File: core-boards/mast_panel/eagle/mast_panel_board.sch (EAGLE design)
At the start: 30 parts, among them J1 2-PIN_2MM-V, J4 4-PIN_2MM-H, U1 ATMEGA328P-AUR, U3 MCP2551T-I/SN

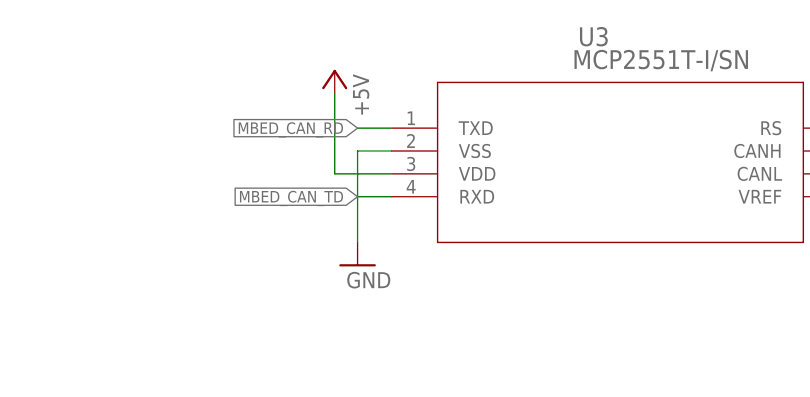
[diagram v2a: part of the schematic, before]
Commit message: 3/1/2020
Switched out CAN connector, cleaned up a few things
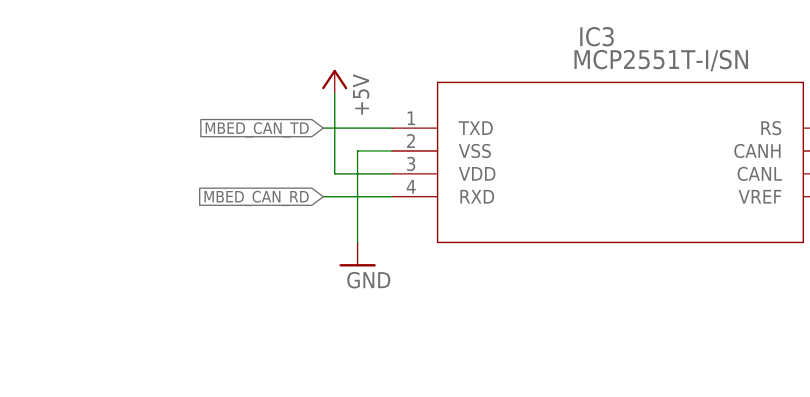
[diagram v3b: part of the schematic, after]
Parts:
- IC3: DIGIKEY (none) -> MCP2551T-I/SNCT-ND
- renumbered U3 to IC3
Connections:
- net MBED_CAN_RD: now also IC3.RXD; no longer IC3.TXD
- net MBED_CAN_TD: now also IC3.TXD; no longer IC3.RXD
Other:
- note added: "CAN Controller"
- note removed: "CAN Bus"
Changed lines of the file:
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@@
 <part name="GND11" library="supply1" library_urn="urn:adsk.eagle:library:371" deviceset="GND" device=""/>
 <part name="GND17" library="supply1" library_urn="urn:adsk.eagle:library:371" deviceset="GND" device=""/>
-<part name="U3" library="MCP2551T" deviceset="MCP2551T-I/SN" device=""/>
 <part name="GND18" library="supply1" library_urn="urn:adsk.eagle:library:371" deviceset="GND" device=""/>
 <part name="GND19" library="supply1" library_urn="urn:adsk.eagle:library:371" deviceset="GND" device=""/>
@@
 <part name="R9" library="rcl" library_urn="urn:adsk.eagle:library:334" deviceset="R-US_" device="R0805" package3d_urn="urn:adsk.eagle:package:23553/2" value="50kO"/>
 <part name="R10" library="rcl" library_urn="urn:adsk.eagle:library:334" deviceset="R-US_" device="R0805" package3d_urn="urn:adsk.eagle:package:23553/2" value="50kO"/>
+<part name="IC3" library="MCP2551T" deviceset="MCP2551T-I/SN" device="">
+<attribute name="DIGIKEY" value="MCP2551T-I/SNCT-ND"/>
+</part>
 </parts>
 <sheets>
@@
 <text x="-64.77" y="-116.84" size="2.54" layer="103" font="vector">LED and Button Connector</text>
 <text x="-63.5" y="45.72" size="2.54" layer="103" font="vector">LCD Connectors</text>
-<text x="1.27" y="52.07" size="2.54" layer="103" font="vector">CAN Bus</text>
 <text x="97.79" y="-62.23" size="2.54" layer="103" font="vector">Power LEDs</text>
 <wire x1="83.82" y1="-54.61" x2="83.82" y2="-105.41" width="0.1524" layer="103" style="shortdash"/>
@@
 <wire x1="71.12" y1="-113.03" x2="1.27" y2="-113.03" width="0.1524" layer="103" style="shortdash"/>
 <text x="2.54" y="-116.84" size="2.54" layer="103" font="vector">ICSP</text>
+<text x="0" y="52.07" size="2.54" layer="103" font="vector">CAN Controller</text>
 </plain>
 <instances>
@@
 <instance part="GND17" gate="1" x="-22.86" y="-107.95" smashed="yes">
 <attribute name="VALUE" x="-24.13" y="-110.49" size="1.778" layer="96"/>
-</instance>
-<instance part="U3" gate="A" x="21.59" y="43.18" smashed="yes">
-<attribute name="NAME" x="44.8056" y="52.2986" size="2.0828" layer="95" ratio="6" rot="SR0"/>
-<attribute name="VALUE" x="44.1706" y="49.7586" size="2.0828" layer="96" ratio="6" rot="SR0"/>
 </instance>
 <instance part="GND18" gate="1" x="95.25" y="31.75" smashed="yes">
@@
 <attribute name="NAME" x="-49.53" y="-101.3714" size="1.778" layer="95"/>
 <attribute name="VALUE" x="-44.45" y="-106.172" size="1.778" layer="96"/>
+</instance>
+<instance part="IC3" gate="A" x="21.59" y="43.18" smashed="yes">
+<attribute name="NAME" x="44.8056" y="52.2986" size="2.0828" layer="95" ratio="6" rot="SR0"/>
+<attribute name="VALUE" x="44.1706" y="49.7586" size="2.0828" layer="96" ratio="6" rot="SR0"/>
+<attribute name="DIGIKEY" x="21.59" y="43.18" size="1.778" layer="96" display="off"/>
 </instance>
 </instances>
@@
 </segment>
 <segment>
-<pinref part="U3" gate="A" pin="VDD"/>
 <wire x1="24.13" y1="38.1" x2="17.78" y2="38.1" width="0.1524" layer="91"/>
 <wire x1="17.78" y1="38.1" x2="17.78" y2="46.99" width="0.1524" layer="91"/>
 <pinref part="P+16" gate="1" pin="+5V"/>
+<pinref part="IC3" gate="A" pin="VDD"/>
 </segment>
 <segment>
@@
 </segment>
 <segment>
-<pinref part="U3" gate="A" pin="RS"/>
 <wire x1="74.93" y1="43.18" x2="95.25" y2="43.18" width="0.1524" layer="91"/>
 <wire x1="95.25" y1="43.18" x2="95.25" y2="34.29" width="0.1524" layer="91"/>
 <pinref part="GND18" gate="1" pin="GND"/>
-</segment>
-<segment>
-<pinref part="U3" gate="A" pin="VSS"/>
-<wire x1="24.13" y1="40.64" x2="20.32" y2="40.64" width="0.1524" layer="91"/>
-<wire x1="20.32" y1="40.64" x2="20.32" y2="30.48" width="0.1524" layer="91"/>
-<pinref part="GND19" gate="1" pin="GND"/>
+<pinref part="IC3" gate="A" pin="RS"/>
 </segment>
 <segment>
@@
 <pinref part="GND13" gate="1" pin="GND"/>
 </segment>
+<segment>
+<wire x1="24.13" y1="40.64" x2="20.32" y2="40.64" width="0.1524" layer="91"/>
+<wire x1="20.32" y1="40.64" x2="20.32" y2="30.48" width="0.1524" layer="91"/>
+<pinref part="GND19" gate="1" pin="GND"/>
+<pinref part="IC3" gate="A" pin="VSS"/>
+</segment>
 </net>
 <net name="BUTTON" class="0">
@@
 <net name="CAN_N" class="0">
 <segment>
-<pinref part="U3" gate="A" pin="CANL"/>
 <wire x1="74.93" y1="38.1" x2="77.47" y2="38.1" width="0.1524" layer="91"/>
 <label x="77.47" y="38.1" size="1.27" layer="95" xref="yes"/>
+<pinref part="IC3" gate="A" pin="CANL"/>
 </segment>
 <segment>
@@
 <net name="CAN_P" class="0">
 <segment>
-<pinref part="U3" gate="A" pin="CANH"/>
 <wire x1="74.93" y1="40.64" x2="77.47" y2="40.64" width="0.1524" layer="91"/>
 <label x="77.47" y="40.64" size="1.27" layer="95" xref="yes"/>
+<pinref part="IC3" gate="A" pin="CANH"/>
 </segment>
 <segment>
@@
 <net name="MBED_CAN_RD" class="0">
 <segment>
-<pinref part="U3" gate="A" pin="TXD"/>
-<wire x1="24.13" y1="43.18" x2="20.32" y2="43.18" width="0.1524" layer="91"/>
-<label x="20.32" y="43.18" size="1.27" layer="95" rot="R180" xref="yes"/>
-</segment>
-<segment>
 <pinref part="U1" gate="A" pin="PD0_(RXD/PCINT16)"/>
 <wire x1="157.48" y1="-5.08" x2="158.75" y2="-5.08" width="0.1524" layer="91"/>
 <label x="158.75" y="-5.08" size="1.27" layer="95" xref="yes"/>
 </segment>
+<segment>
+<wire x1="24.13" y1="35.56" x2="16.51" y2="35.56" width="0.1524" layer="91"/>
+<label x="16.51" y="35.56" size="1.27" layer="95" rot="R180" xref="yes"/>
+<pinref part="IC3" gate="A" pin="RXD"/>
+</segment>
 </net>
 <net name="MBED_CAN_TD" class="0">
-<segment>
-<pinref part="U3" gate="A" pin="RXD"/>
-<wire x1="24.13" y1="35.56" x2="20.32" y2="35.56" width="0.1524" layer="91"/>
-<label x="20.32" y="35.56" size="1.27" layer="95" rot="R180" xref="yes"/>
-</segment>
 <segment>
 <pinref part="U1" gate="A" pin="PD1_(TXD/PCINT17)"/>
@@
 <label x="158.75" y="-2.54" size="1.27" layer="95" xref="yes"/>
 </segment>
-</net>
+<segment>
+<wire x1="24.13" y1="43.18" x2="16.51" y2="43.18" width="0.1524" layer="91"/>
+<pinref part="IC3" gate="A" pin="TXD"/>
+<label x="16.51" y="43.18" size="1.27" layer="95" rot="R180" xref="yes"/>
+</segment>
+</net>

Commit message: Revert "3/1/2020"
This reverts commit 3611e6968998cfd50a97478803bccb5be4cedb33.
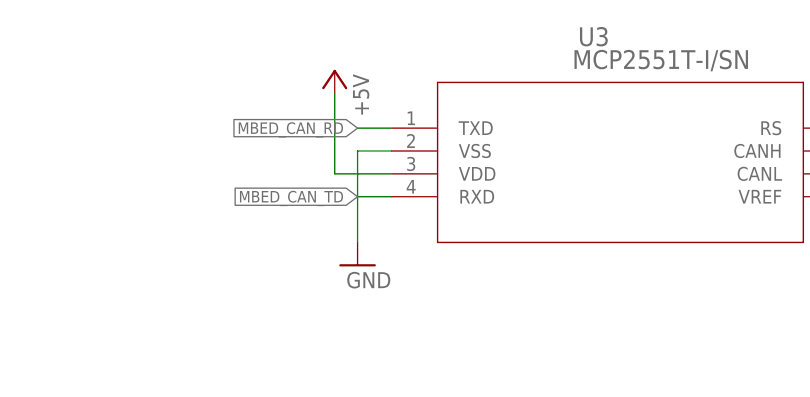
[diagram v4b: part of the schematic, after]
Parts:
- U3: DIGIKEY MCP2551T-I/SNCT-ND -> (none)
- renumbered IC3 to U3
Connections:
- net MBED_CAN_RD: now also U3.TXD; no longer U3.RXD
- net MBED_CAN_TD: now also U3.RXD; no longer U3.TXD
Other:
- note added: "CAN Bus"
- note removed: "CAN Controller"
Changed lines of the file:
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@@
 <part name="GND11" library="supply1" library_urn="urn:adsk.eagle:library:371" deviceset="GND" device=""/>
 <part name="GND17" library="supply1" library_urn="urn:adsk.eagle:library:371" deviceset="GND" device=""/>
+<part name="U3" library="MCP2551T" deviceset="MCP2551T-I/SN" device=""/>
 <part name="GND18" library="supply1" library_urn="urn:adsk.eagle:library:371" deviceset="GND" device=""/>
 <part name="GND19" library="supply1" library_urn="urn:adsk.eagle:library:371" deviceset="GND" device=""/>
@@
 <part name="R9" library="rcl" library_urn="urn:adsk.eagle:library:334" deviceset="R-US_" device="R0805" package3d_urn="urn:adsk.eagle:package:23553/2" value="50kO"/>
 <part name="R10" library="rcl" library_urn="urn:adsk.eagle:library:334" deviceset="R-US_" device="R0805" package3d_urn="urn:adsk.eagle:package:23553/2" value="50kO"/>
-<part name="IC3" library="MCP2551T" deviceset="MCP2551T-I/SN" device="">
-<attribute name="DIGIKEY" value="MCP2551T-I/SNCT-ND"/>
-</part>
 </parts>
 <sheets>
@@
 <text x="-64.77" y="-116.84" size="2.54" layer="103" font="vector">LED and Button Connector</text>
 <text x="-63.5" y="45.72" size="2.54" layer="103" font="vector">LCD Connectors</text>
+<text x="1.27" y="52.07" size="2.54" layer="103" font="vector">CAN Bus</text>
 <text x="97.79" y="-62.23" size="2.54" layer="103" font="vector">Power LEDs</text>
 <wire x1="83.82" y1="-54.61" x2="83.82" y2="-105.41" width="0.1524" layer="103" style="shortdash"/>
@@
 <wire x1="71.12" y1="-113.03" x2="1.27" y2="-113.03" width="0.1524" layer="103" style="shortdash"/>
 <text x="2.54" y="-116.84" size="2.54" layer="103" font="vector">ICSP</text>
-<text x="0" y="52.07" size="2.54" layer="103" font="vector">CAN Controller</text>
 </plain>
 <instances>
@@
 <instance part="GND17" gate="1" x="-22.86" y="-107.95" smashed="yes">
 <attribute name="VALUE" x="-24.13" y="-110.49" size="1.778" layer="96"/>
+</instance>
+<instance part="U3" gate="A" x="21.59" y="43.18" smashed="yes">
+<attribute name="NAME" x="44.8056" y="52.2986" size="2.0828" layer="95" ratio="6" rot="SR0"/>
+<attribute name="VALUE" x="44.1706" y="49.7586" size="2.0828" layer="96" ratio="6" rot="SR0"/>
 </instance>
 <instance part="GND18" gate="1" x="95.25" y="31.75" smashed="yes">
@@
 <attribute name="NAME" x="-49.53" y="-101.3714" size="1.778" layer="95"/>
 <attribute name="VALUE" x="-44.45" y="-106.172" size="1.778" layer="96"/>
-</instance>
-<instance part="IC3" gate="A" x="21.59" y="43.18" smashed="yes">
-<attribute name="NAME" x="44.8056" y="52.2986" size="2.0828" layer="95" ratio="6" rot="SR0"/>
-<attribute name="VALUE" x="44.1706" y="49.7586" size="2.0828" layer="96" ratio="6" rot="SR0"/>
-<attribute name="DIGIKEY" x="21.59" y="43.18" size="1.778" layer="96" display="off"/>
 </instance>
 </instances>
@@
 </segment>
 <segment>
+<pinref part="U3" gate="A" pin="VDD"/>
 <wire x1="24.13" y1="38.1" x2="17.78" y2="38.1" width="0.1524" layer="91"/>
 <wire x1="17.78" y1="38.1" x2="17.78" y2="46.99" width="0.1524" layer="91"/>
 <pinref part="P+16" gate="1" pin="+5V"/>
-<pinref part="IC3" gate="A" pin="VDD"/>
 </segment>
 <segment>
@@
 </segment>
 <segment>
+<pinref part="U3" gate="A" pin="RS"/>
 <wire x1="74.93" y1="43.18" x2="95.25" y2="43.18" width="0.1524" layer="91"/>
 <wire x1="95.25" y1="43.18" x2="95.25" y2="34.29" width="0.1524" layer="91"/>
 <pinref part="GND18" gate="1" pin="GND"/>
-<pinref part="IC3" gate="A" pin="RS"/>
+</segment>
+<segment>
+<pinref part="U3" gate="A" pin="VSS"/>
+<wire x1="24.13" y1="40.64" x2="20.32" y2="40.64" width="0.1524" layer="91"/>
+<wire x1="20.32" y1="40.64" x2="20.32" y2="30.48" width="0.1524" layer="91"/>
+<pinref part="GND19" gate="1" pin="GND"/>
 </segment>
 <segment>
@@
 <pinref part="GND13" gate="1" pin="GND"/>
 </segment>
-<segment>
-<wire x1="24.13" y1="40.64" x2="20.32" y2="40.64" width="0.1524" layer="91"/>
-<wire x1="20.32" y1="40.64" x2="20.32" y2="30.48" width="0.1524" layer="91"/>
-<pinref part="GND19" gate="1" pin="GND"/>
-<pinref part="IC3" gate="A" pin="VSS"/>
-</segment>
 </net>
 <net name="BUTTON" class="0">
@@
 <net name="CAN_N" class="0">
 <segment>
+<pinref part="U3" gate="A" pin="CANL"/>
 <wire x1="74.93" y1="38.1" x2="77.47" y2="38.1" width="0.1524" layer="91"/>
 <label x="77.47" y="38.1" size="1.27" layer="95" xref="yes"/>
-<pinref part="IC3" gate="A" pin="CANL"/>
 </segment>
 <segment>
@@
 <net name="CAN_P" class="0">
 <segment>
+<pinref part="U3" gate="A" pin="CANH"/>
 <wire x1="74.93" y1="40.64" x2="77.47" y2="40.64" width="0.1524" layer="91"/>
 <label x="77.47" y="40.64" size="1.27" layer="95" xref="yes"/>
-<pinref part="IC3" gate="A" pin="CANH"/>
 </segment>
 <segment>
@@
 <net name="MBED_CAN_RD" class="0">
 <segment>
+<pinref part="U3" gate="A" pin="TXD"/>
+<wire x1="24.13" y1="43.18" x2="20.32" y2="43.18" width="0.1524" layer="91"/>
+<label x="20.32" y="43.18" size="1.27" layer="95" rot="R180" xref="yes"/>
+</segment>
+<segment>
 <pinref part="U1" gate="A" pin="PD0_(RXD/PCINT16)"/>
 <wire x1="157.48" y1="-5.08" x2="158.75" y2="-5.08" width="0.1524" layer="91"/>
 <label x="158.75" y="-5.08" size="1.27" layer="95" xref="yes"/>
 </segment>
-<segment>
-<wire x1="24.13" y1="35.56" x2="16.51" y2="35.56" width="0.1524" layer="91"/>
-<label x="16.51" y="35.56" size="1.27" layer="95" rot="R180" xref="yes"/>
-<pinref part="IC3" gate="A" pin="RXD"/>
-</segment>
 </net>
 <net name="MBED_CAN_TD" class="0">
+<segment>
+<pinref part="U3" gate="A" pin="RXD"/>
+<wire x1="24.13" y1="35.56" x2="20.32" y2="35.56" width="0.1524" layer="91"/>
+<label x="20.32" y="35.56" size="1.27" layer="95" rot="R180" xref="yes"/>
+</segment>
 <segment>
 <pinref part="U1" gate="A" pin="PD1_(TXD/PCINT17)"/>
@@
 <label x="158.75" y="-2.54" size="1.27" layer="95" xref="yes"/>
 </segment>
-<segment>
-<wire x1="24.13" y1="43.18" x2="16.51" y2="43.18" width="0.1524" layer="91"/>
-<pinref part="IC3" gate="A" pin="TXD"/>
-<label x="16.51" y="43.18" size="1.27" layer="95" rot="R180" xref="yes"/>
-</segment>
-</net>
+</net>
